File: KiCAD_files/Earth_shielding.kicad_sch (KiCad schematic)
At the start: 10 parts

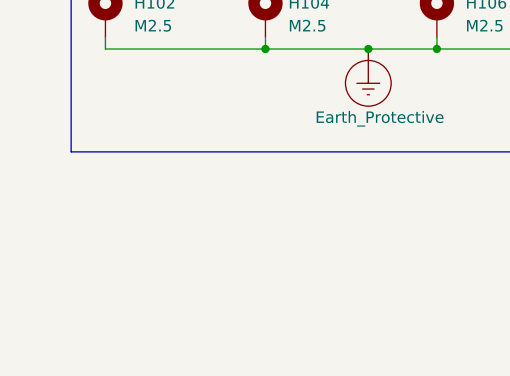
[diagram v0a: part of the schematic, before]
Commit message: removed power ports on hierarchical blocks
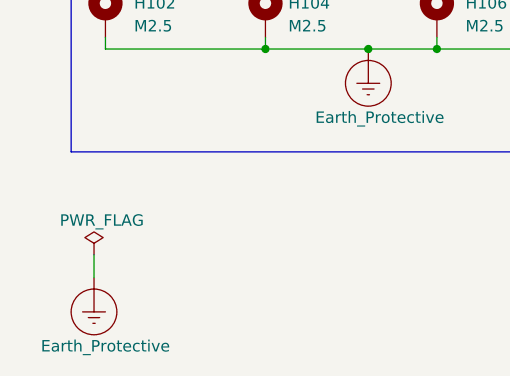
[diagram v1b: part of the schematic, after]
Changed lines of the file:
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@@
+    (stroke (width 0) (type default))
+  )
+  (wire (pts (xy 139.7 134.62) (xy 139.7 137.16))
     (stroke (width 0) (type default))
   )
@@
     )
   )
+  (symbol (lib_id "power:Earth_Protective") (at 139.7 137.16 0) (unit 1)
+    (in_bom yes) (on_board yes) (dnp no)
+    (property "Reference" "#PWR0114" (at 146.05 143.51 0)
+      (effects (font (size 1.27 1.27)) hide)
+    )
+    (property "Value" "Earth_Protective" (at 140.97 144.78 0)
+      (effects (font (size 1.27 1.27)))
+    )
+    (property "Footprint" "" (at 139.7 139.7 0)
+      (effects (font (size 1.27 1.27)) hide)
+    )
+    (property "Datasheet" "~" (at 139.7 139.7 0)
+      (effects (font (size 1.27 1.27)) hide)
+    )
+    (pin "1")
+    (instances
+      (project "inverter"
+        (path "/8d0c1d66-35ef-4a53-a28f-436a11b54f42"
+          (reference "#PWR0114") (unit 1)
+        )
+        (path "/8d0c1d66-35ef-4a53-a28f-436a11b54f42/d8e0f3be-356c-4f17-abdf-62f1abb3dd16"
+          (reference "#PWR0130") (unit 1)
+        )
+      )
+    )
+  )
   (symbol (lib_id "Mechanical:MountingHole_Pad") (at 195.58 107.95 0) (unit 1)
     (in_bom yes) (on_board yes) (dnp no) (fields_autoplaced)
@@
         )
       )
+    )
+  )
+  (symbol (lib_id "power:PWR_FLAG") (at 139.7 134.62 0) (unit 1)
+    (in_bom yes) (on_board yes) (dnp no)
+    (property "Reference" "#FLG0101" (at 139.7 132.715 0)
+      (effects (font (size 1.27 1.27)) hide)
+    )
+    (property "Value" "PWR_FLAG" (at 135.89 130.81 0)
+      (effects (font (size 1.27 1.27)) (justify left))
+    )
+    (property "Footprint" "" (at 139.7 134.62 0)
+      (effects (font (size 1.27 1.27)) hide)
+    )
+    (property "Datasheet" "~" (at 139.7 134.62 0)
+      (effects (font (size 1.27 1.27)) hide)
+    )
+    (pin "1")
+    (instances
+      (project "inverter"
+        (path "/8d0c1d66-35ef-4a53-a28f-436a11b54f42"
+          (reference "#FLG0101") (unit 1)
+        )
+        (path "/8d0c1d66-35ef-4a53-a28f-436a11b54f42/d8e0f3be-356c-4f17-abdf-62f1abb3dd16"
+          (reference "#FLG0104") (unit 1)
+        )
+      )

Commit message: save before starting routing
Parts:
- renumbered H101 to H?, H107 to H?, H108 to H?, H106 to H?, H104 to H?, H105 to H?, H109 to H?, H102 to H?, H103 to H?, N101 to N?
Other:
- title: (none) -> OWNVERTER V0.1

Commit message: real before importing netlist
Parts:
- removed H? (x9): M2.5, MountingHole:MountingHole_2.7mm_M2.5_DIN965_Pad_TopOnly, symbol Mechanical:MountingHole_Pad
- removed N?: Housing_Pad, Footprints:Guard_ring, symbol Mechanical:Housing_Pad
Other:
- note removed: "EARTH AREA"
- note removed: "Earth shielding"
